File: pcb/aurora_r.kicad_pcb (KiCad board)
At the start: 2 copper layers, 182.9 x 107.7 mm, 125 parts

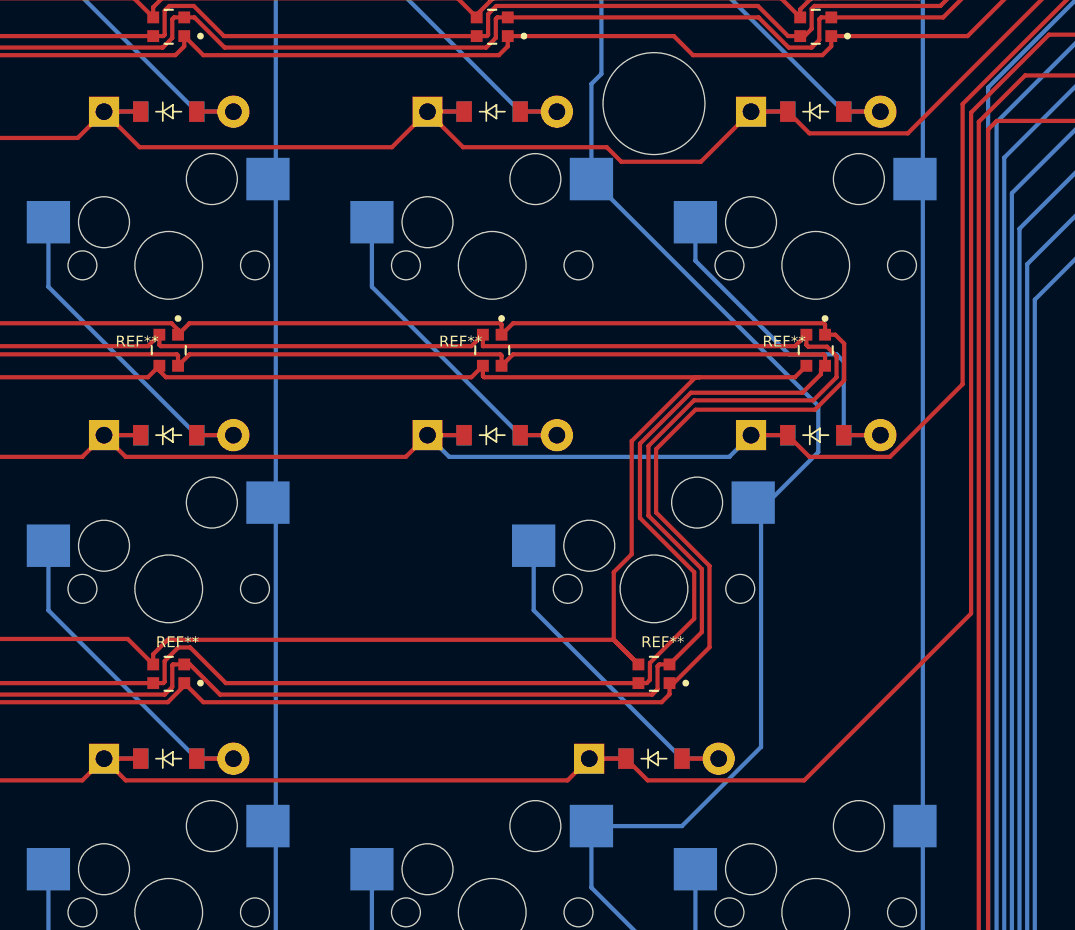
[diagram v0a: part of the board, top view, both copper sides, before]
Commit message: Add stab holes to PCBs
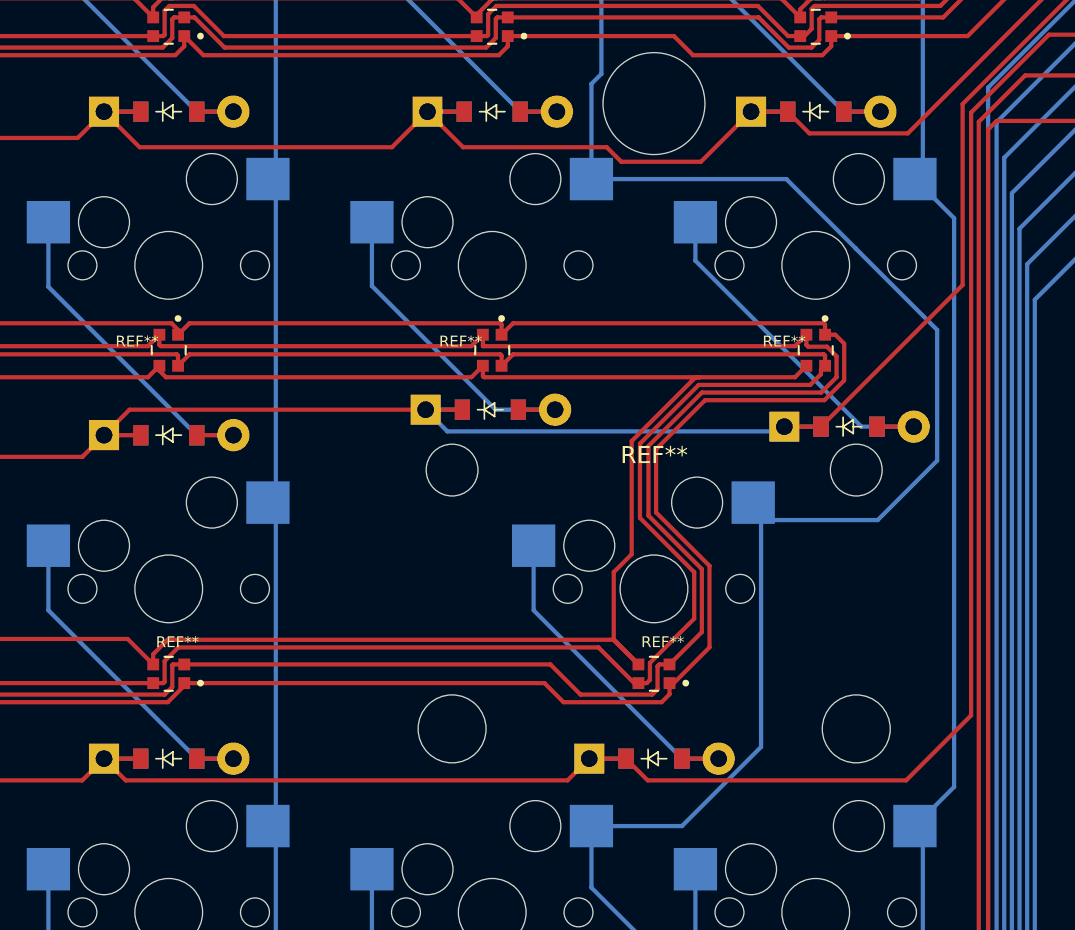
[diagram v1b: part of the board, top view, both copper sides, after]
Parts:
- added REF**: SW_Cherry_MX_2.00u_PCB, Button_Switch_Keyboard:SW_Cherry_MX_2.00u_PCB, F.Cu at (226.4, 114.0)
- moved D15 2.02 mm to (235.3, 109.5)
- moved D13 1.50 mm to (214.2, 108.5)
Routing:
- net P020: track 236.4 -> 254.2 mm
- net P029: track 231.5 -> 225.9 mm
- net P002: track 242.5 -> 246.0 mm
- net P017: track 90.4 -> 91.9 mm
- net eight_top: track 22.1 -> 21.3 mm
- net seven_top: track 20.5 -> 19.7 mm

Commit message: Minor adjustment to left pcb
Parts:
- turned JST1 to 180 degrees
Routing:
- net GND: track 999.3 -> 995.0 mm
- net BAT: track 17.0 -> 18.1 mm
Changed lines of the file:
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@@
 			(outputformat 1)
 			(mirror no)
-			(drillshape 1)
+			(drillshape 0)
 			(scaleselection 1)
-			(outputdirectory "")
+			(outputdirectory "C:/Users/Musab/Desktop/right-gerber/")
 		)
 	)
@@
 	(footprint "JST_PH_S2B-PH-K_02x2.00mm_Angled"
 		(layer "F.Cu")
-		(at 267.64 114.2875)
+		(at 267.64 114.2875 180)
 		(descr "JST PH series connector, S2B-PH-K, side entry type, through hole, Datasheet: http://www.jst-mfg.com/product/pdf/eng/ePH.pdf")
 		(tags "connector jst ph")
@@
 		(attr through_hole)
 		(fp_line
-			(start -2.95 -1.35)
-			(end -2.95 6.25)
+			(start 2.95 6.25)
+			(end 2.95 -1.35)
 			(stroke
 				(width 0.15)
@@
 		)
 		(fp_line
-			(start -2.95 6.25)
-			(end 2.95 6.25)
+			(start 2.95 -1.35)
+			(end 2.25 -1.35)
 			(stroke
 				(width 0.15)
@@
 		)
 		(fp_line
-			(start -2.25 -1.35)
-			(end -2.95 -1.35)
+			(start 2.25 0.25)
+			(end -2.25 0.25)
 			(stroke
 				(width 0.15)
@@
 		)
 		(fp_line
-			(start -2.25 0.25)
-			(end -2.25 -1.35)
+			(start 2.25 -1.35)
+			(end 2.25 0.25)
 			(stroke
 				(width 0.15)
@@
 		)
 		(fp_line
-			(start -1.25 1.75)
-			(end -0.75 1.75)
+			(start -1 1.5)
+			(end -1 2)
 			(stroke
 				(width 0.15)
@@
 		)
 		(fp_line
-			(start -1 1.5)
-			(end -1 2)
+			(start -1.25 1.75)
+			(end -0.75 1.75)
 			(stroke
 				(width 0.15)
@@
 		)
 		(fp_line
-			(start 2.25 -1.35)
-			(end 2.25 0.25)
+			(start -2.25 0.25)
+			(end -2.25 -1.35)
 			(stroke
 				(width 0.15)
@@
 		)
 		(fp_line
-			(start 2.25 0.25)
-			(end -2.25 0.25)
+			(start -2.25 -1.35)
+			(end -2.95 -1.35)
 			(stroke
 				(width 0.15)
@@
 		)
 		(fp_line
-			(start 2.95 -1.35)
-			(end 2.25 -1.35)
+			(start -2.95 6.25)
+			(end 2.95 6.25)
 			(stroke
 				(width 0.15)
@@
 		)
 		(fp_line
-			(start 2.95 6.25)
-			(end 2.95 -1.35)
+			(start -2.95 -1.35)
+			(end -2.95 6.25)
 			(stroke
 				(width 0.15)
@@
 		)
 		(pad "1" thru_hole rect
-			(at -1 0)
+			(at -1 0 180)
 			(size 1.2 1.7)
 			(drill 0.75)
@@
 		)
 		(pad "2" thru_hole oval
-			(at 1 0)
+			(at 1 0 180)
 			(size 1.2 1.7)
 			(drill 0.75)
@@
 	)
 	(segment
-		(start 250.447405 68.1862)
-		(end 249 69.633605)
+		(start 270.776 110.1515)
+		(end 270.776 107.3875)
 		(width 0.25)
 		(layer "B.Cu")
@@
 	)
 	(segment
-		(start 249 69.633605)
-		(end 249 73.4225)
+		(start 250.447405 68.1862)
+		(end 249 69.633605)
 		(width 0.25)
 		(layer "B.Cu")
@@
 	)
 	(segment
-		(start 270.751 130.749)
-		(end 269.601 131.899)
+		(start 269.601 117.2485)
+		(end 269.601 126.2)
 		(width 0.25)
 		(layer "B.Cu")
@@
 	)
 	(segment
-		(start 270.051 126.033274)
-		(end 270.751 126.733274)
+		(start 249 69.633605)
+		(end 249 73.4225)
 		(width 0.25)
 		(layer "B.Cu")
@@
 	)
 	(segment
-		(start 270.776 112.1515)
-		(end 270.776 107.3875)
-		(width 0.25)
-		(layer "B.Cu")
-		(net 55)
-	)
-	(segment
 		(start 266.232595 76.1188)
 		(end 265.237405 76.1188)
@@
 	)
 	(segment
-		(start 270.751 126.733274)
-		(end 270.751 130.749)
-		(width 0.25)
-		(layer "B.Cu")
-		(net 55)
-	)
-	(segment
 		(start 266.9363 73.5788)
 		(end 265.735 72.3775)
@@
 	)
 	(segment
-		(start 260.655 133.05)
-		(end 257.48 129.875)
-		(width 0.25)
-		(layer "B.Cu")
-		(net 55)
-	)
-	(segment
-		(start 268.64 114.2875)
-		(end 270.051 115.6985)
-		(width 0.25)
-		(layer "B.Cu")
-		(net 55)
-	)
-	(segment
 		(start 257.48 126.59)
 		(end 252.4 121.51)
@@
 	)
 	(segment
-		(start 269.601 131.899)
-		(end 269.601 133.05)
+		(start 266.568351 128.882649)
+		(end 267.8005 127.6505)
 		(width 0.25)
 		(layer "B.Cu")
@@
 	)
 	(segment
+		(start 266.568351 130.068351)
+		(end 266.568351 128.882649)
+		(width 0.25)
+		(layer "B.Cu")
+		(net 55)
+	)
+	(segment
 		(start 270.776 102.1375)
 		(end 270.551 102.3625)
@@
 	)
 	(segment
+		(start 258.655 131.05)
+		(end 257.48 129.875)
+		(width 0.25)
+		(layer "B.Cu")
+		(net 55)
+	)
+	(segment
 		(start 250.495 74.9175)
 		(end 250.495 77.4575)
@@
 	)
 	(segment
-		(start 268.64 114.2875)
-		(end 270.776 112.1515)
+		(start 257.932405 68.1862)
+		(end 266.418991 68.1862)
 		(width 0.25)
 		(layer "B.Cu")
@@
 	)
 	(segment
-		(start 257.932405 68.1862)
-		(end 266.418991 68.1862)
+		(start 265.586701 131.05)
+		(end 258.655 131.05)
 		(width 0.25)
 		(layer "B.Cu")
@@
 	)
 	(segment
+		(start 267.8005 127.6505)
+		(end 268.1505 127.6505)
+		(width 0.25)
+		(layer "B.Cu")
+		(net 55)
+	)
+	(segment
 		(start 270.776 101.9125)
 		(end 270.776 102.1375)
@@
 	)
 	(segment
-		(start 270.051 115.6985)
-		(end 270.051 126.033274)
+		(start 266.568351 130.068351)
+		(end 265.586701 131.05)
+		(width 0.25)
+		(layer "B.Cu")
+		(net 55)
+	)
+	(segment
+		(start 266.64 114.2875)
+		(end 270.776 110.1515)
 		(width 0.25)
 		(layer "B.Cu")
@@
 	)
 	(segment
+		(start 266.64 114.2875)
+		(end 269.601 117.2485)
+		(width 0.25)
+		(layer "B.Cu")
+		(net 55)
+	)
+	(segment
 		(start 269.526 100.6625)
 		(end 270.776 101.9125)
@@
 	)
 	(segment
-		(start 269.601 133.05)
-		(end 260.655 133.05)
+		(start 269.601 126.2)
+		(end 268.1505 127.6505)
 		(width 0.25)
 		(layer "B.Cu")
@@
 	)
 	(segment
-		(start 269.601 117.2485)
-		(end 269.601 126.233273)
+		(start 270.251 115.8985)
+		(end 270.251 126.233274)
 		(width 0.25)
 		(layer "B.Cu")
@@
 	)
 	(segment
-		(start 266.64 114.2875)
-		(end 269.601 117.2485)
+		(start 271 127.5)
+		(end 269.175 129.325)
 		(width 0.25)
 		(layer "B.Cu")
@@
 	)
 	(segment
-		(start 267.851 127.983273)
+		(start 270.251 126.233274)
+		(end 271 126.982274)
+		(width 0.25)
+		(layer "B.Cu")
+		(net 64)
+	)
+	(segment
+		(start 269.175 129.325)
 		(end 267.851 129.325)
 		(width 0.25)
@@
 	)
 	(segment
-		(start 269.601 126.233273)
-		(end 267.851 127.983273)
+		(start 268.64 114.2875)
+		(end 270.251 115.8985)
+		(width 0.25)
+		(layer "B.Cu")
+		(net 64)
+	)
+	(segment
+		(start 271 126.982274)
+		(end 271 127.5)
 		(width 0.25)
 		(layer "B.Cu")

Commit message: Rotary encoder pinout fixes
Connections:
- ROT1 pad 1: (no net) -> P111
- ROT1 pad 2: (no net) -> GND
- ROT1 pad B: GND -> P008
- ROT1 pad C: P008 -> GND
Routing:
- net P111: track 0.00 -> 25.3 mm
- net GND: track 995.0 -> 1002.9 mm
- net P008: track 47.9 -> 50.4 mm
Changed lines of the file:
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@@
 			(layers "*.Cu" "*.Mask")
 			(remove_unused_layers no)
+			(net 58 "P111")
 		)
 		(pad "2" thru_hole circle
@@
 			(layers "*.Cu" "*.Mask")
 			(remove_unused_layers no)
+			(net 55 "GND")
 		)
 		(pad "A" thru_hole rect
@@
 			(layers "*.Cu" "*.Mask")
 			(remove_unused_layers no)
-			(net 55 "GND")
+			(net 60 "P008")
 		)
 		(pad "C" thru_hole circle
@@
 			(layers "*.Cu" "*.Mask")
 			(remove_unused_layers no)
-			(net 60 "P008")
+			(net 55 "GND")
 		)
 	)
@@
 	)
 	(segment
+		(start 269.601 117.2485)
+		(end 269.601 121.5)
+		(width 0.25)
+		(layer "B.Cu")
+		(net 55)
+	)
+	(segment
 		(start 270.776 110.1515)
 		(end 270.776 107.3875)
@@
 	)
 	(segment
+		(start 252.4 119.01)
+		(end 257.48 124.09)
+		(width 0.25)
+		(layer "B.Cu")
+		(net 55)
+	)
+	(segment
 		(start 250.447405 68.1862)
 		(end 249 69.633605)
@@
 	)
 	(segment
-		(start 269.601 117.2485)
+		(start 269.601 121.5)
 		(end 269.601 126.2)
 		(width 0.25)
@@
 	)
 	(segment
+		(start 269.591 121.51)
+		(end 269.601 121.5)
+		(width 0.25)
+		(layer "B.Cu")
+		(net 55)
+	)
+	(segment
 		(start 266.9363 73.5788)
 		(end 265.735 72.3775)
@@
 	)
 	(segment
-		(start 257.48 126.59)
-		(end 252.4 121.51)
+		(start 266.9 121.51)
+		(end 269.601 118.809)
 		(width 0.25)
 		(layer "B.Cu")
@@
 	)
 	(segment
-		(start 257.48 129.875)
-		(end 257.48 126.59)
-		(width 0.25)
-		(layer "B.Cu")
-		(net 55)
-	)
-	(segment
 		(start 258.655 131.05)
 		(end 257.48 129.875)
@@
 	)
 	(segment
+		(start 257.48 124.09)
+		(end 257.48 129.875)
+		(width 0.25)
+		(layer "B.Cu")
+		(net 55)
+	)
+	(segment
 		(start 266.568351 130.068351)
 		(end 265.586701 131.05)
@@
 	)
 	(segment
+		(start 269.601 118.809)
+		(end 269.601 117.2485)
+		(width 0.25)
+		(layer "B.Cu")
+		(net 55)
+	)
+	(segment
 		(start 264 122.474)
 		(end 264 102.5)
@@
 	)
 	(segment
+		(start 265.735 92.6975)
+		(end 264.5337 93.8988)
+		(width 0.25)
+		(layer "F.Cu")
+		(net 58)
+	)
+	(segment
+		(start 264.5337 114.1437)
+		(end 266.9 116.51)
+		(width 0.25)
+		(layer "F.Cu")
+		(net 58)
+	)
+	(segment
+		(start 264.5337 93.8988)
+		(end 264.5337 114.1437)
+		(width 0.25)
+		(layer "F.Cu")
+		(net 58)
+	)
+	(segment
 		(start 252.1463 71.4888)
 		(end 250.495 69.8375)
@@
 	)
 	(segment
-		(start 251.075 117.685)
-		(end 252.4 119.01)
+		(start 250.495 72.3775)
+		(end 251.6963 73.5788)
 		(width 0.25)
 		(layer "B.Cu")
@@
 	)
 	(segment
-		(start 251.075 115)
-		(end 251.075 117.685)
+		(start 251.6963 73.5788)
+		(end 251.6963 114.3787)
 		(width 0.25)
 		(layer "B.Cu")
@@
 	)
 	(segment
-		(start 251.6963 73.5788)
-		(end 251.6963 114.3787)
+		(start 251.075 120.185)
+		(end 252.4 121.51)
 		(width 0.25)
 		(layer "B.Cu")
@@
 	)
 	(segment
-		(start 250.495 72.3775)
-		(end 251.6963 73.5788)
+		(start 251.075 115)
+		(end 251.075 120.185)
 		(width 0.25)
 		(layer "B.Cu")

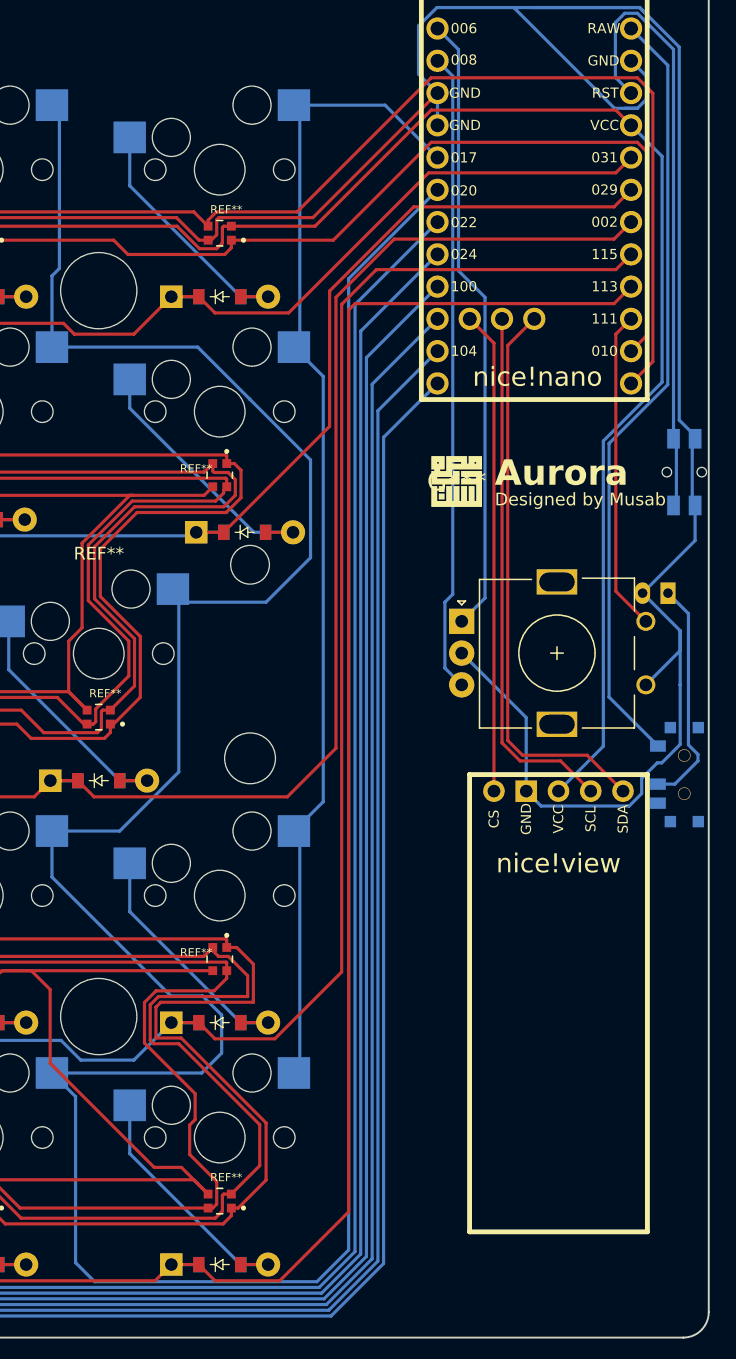
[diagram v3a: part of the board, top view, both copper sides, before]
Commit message: Pin changes on encoder button
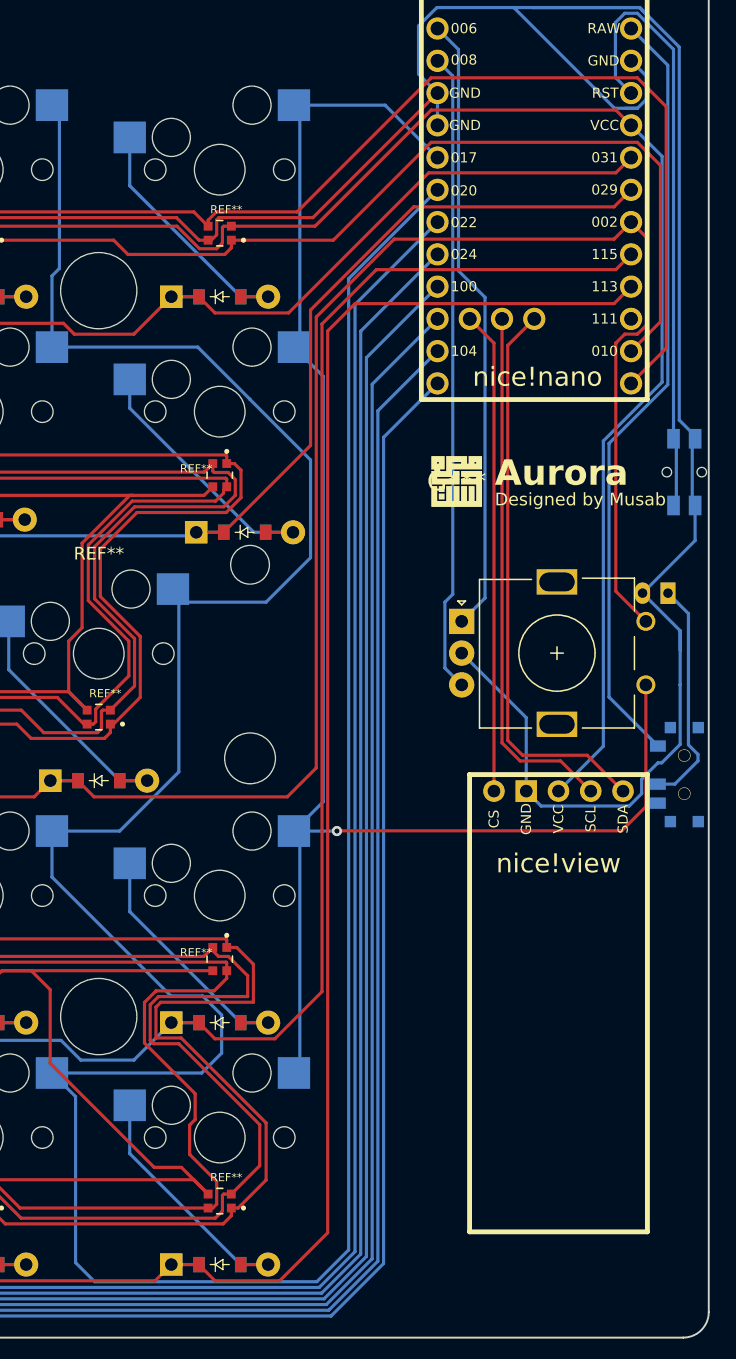
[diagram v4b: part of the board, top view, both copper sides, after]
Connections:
- ROT1 pad 1: P111 -> P002
- ROT1 pad 2: GND -> P017
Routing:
- net P017: track 91.9 -> 130.0 mm, vias 0 -> 1
- net P002: track 246.0 -> 280.6 mm
- net P111: track 25.3 -> 0.00 mm
- net GND: track 1002.9 -> 999.1 mm
- net P009: track 865.9 -> 866.7 mm
- net P010: track 871.4 -> 872.3 mm
